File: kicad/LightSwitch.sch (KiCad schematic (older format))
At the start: 20 parts

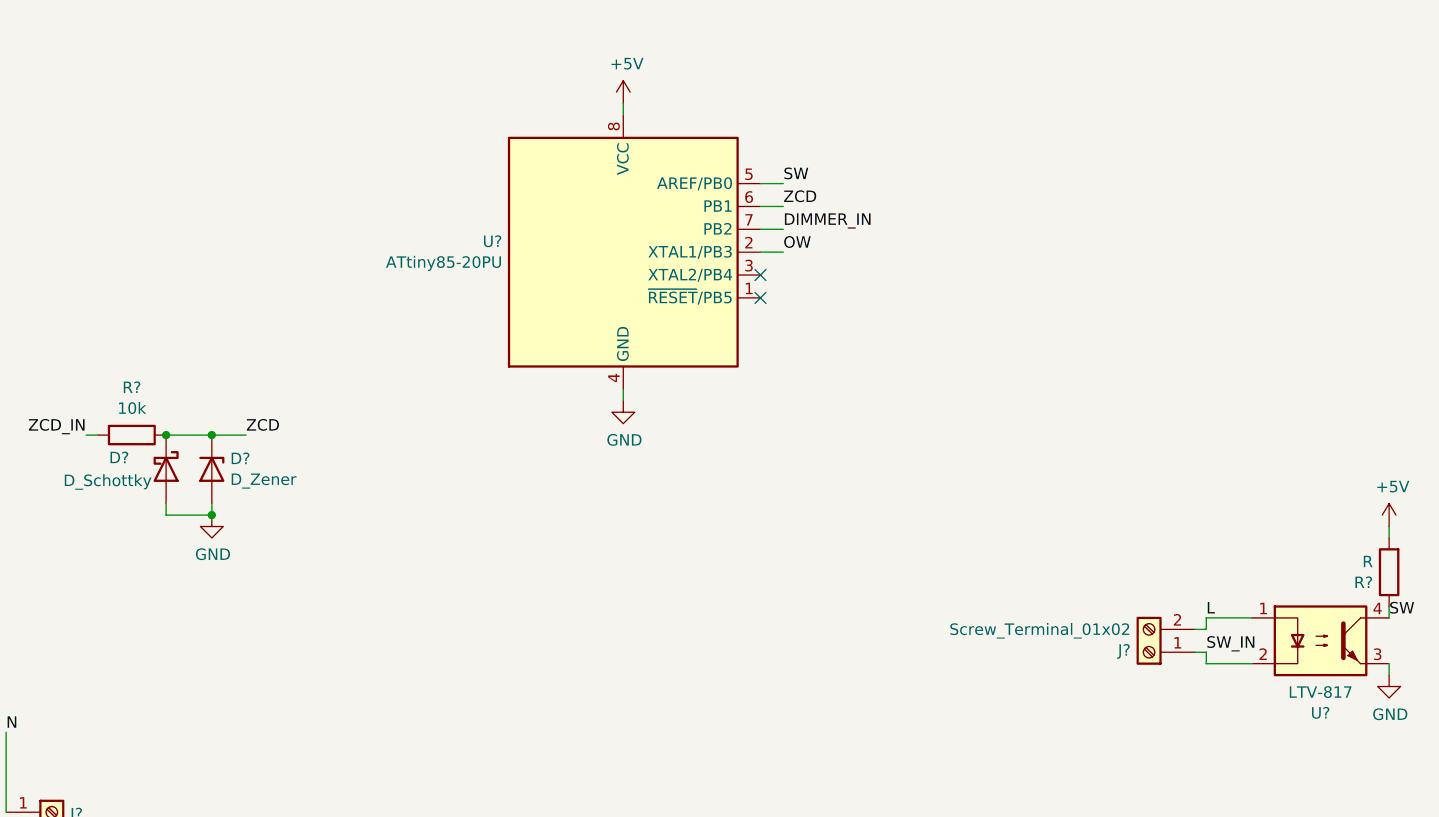
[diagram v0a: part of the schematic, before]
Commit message: Some small circuit changes
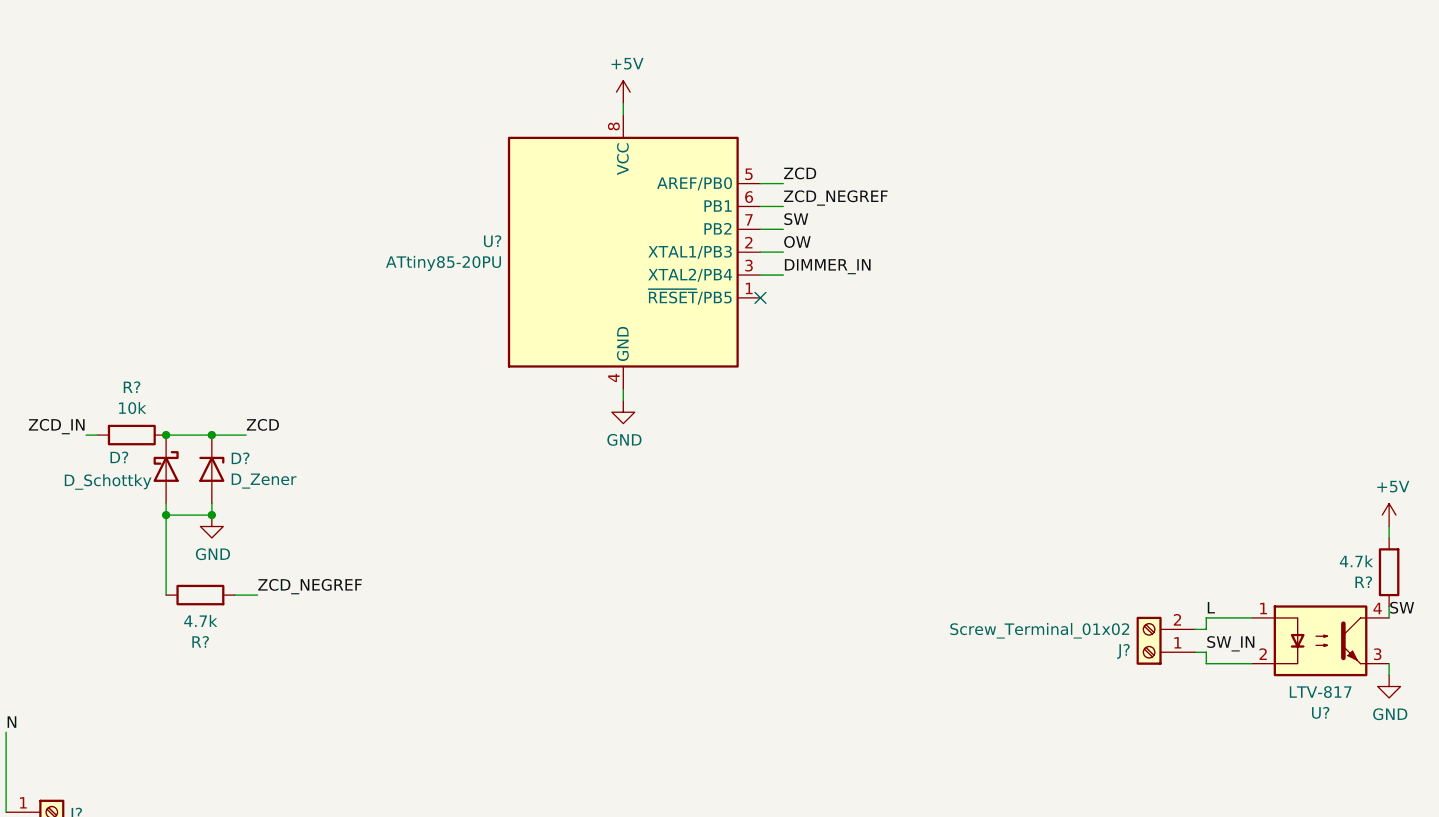
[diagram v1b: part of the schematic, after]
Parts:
- added R?: 4.7k, symbol Device:R
- R?: value R -> 4.7k
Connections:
- net DIMMER_IN: now also U?.3 (XTAL2/PB4); no longer U?.7 (PB2)
- net GND: now also R?.1
- net SW: now also U?.7 (PB2); no longer U?.5 (AREF/PB0)
- net ZCD: now also U?.5 (AREF/PB0); no longer U?.6 (PB1)
- new net ZCD_NEGREF: R?.2, U?.6 (PB1)
- no-connect marks 2 -> 1
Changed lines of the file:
@@
 Wire Wire Line
 	6650 1250 6650 1300
+Text Label 7350 1800 0    50   ~ 0
+SW
+Wire Wire Line
+	7250 1600 7350 1600
 Text Label 7350 1600 0    50   ~ 0
-SW
-Wire Wire Line
-	7250 1600 7350 1600
-Text Label 7350 1700 0    50   ~ 0
 ZCD
-Wire Wire Line
-	7350 1700 7250 1700
 $Comp
 L Relay_SolidState:MOC3052M U?
@@
 Wire Wire Line
 	2000 4250 2050 4250
-Text Label 7350 1800 0    50   ~ 0
+Text Label 7350 2000 0    50   ~ 0
 DIMMER_IN
 Wire Wire Line
@@
 	7350 1900 7250 1900
 NoConn ~ 7250 2100
-NoConn ~ 7250 2000
 $Comp
 L Connector:Screw_Terminal_01x02 J?
@@
 P 10000 3300
 F 0 "R?" H 10070 3346 50  0000 L CNN
-F 1 "R" H 10070 3255 50  0000 L CNN
+F 1 "4.7k" H 10070 3255 50  0000 L CNN
 F 2 "" V 9930 3300 50  0001 C CNN
 F 3 "~" H 10000 3300 50  0001 C CNN
@@
 Wire Wire Line
 	4850 2700 5000 2700
+$Comp
+L Device:R R?
+U 1 1 61ADD4D7
+P 4800 3400
+F 0 "R?" V 4593 3400 50  0000 C CNN
+F 1 "4.7k" V 4684 3400 50  0000 C CNN
+F 2 "" V 4730 3400 50  0001 C CNN
+F 3 "~" H 4800 3400 50  0001 C CNN
+	1    4800 3400
+	0    -1   -1   0
+$EndComp
+Wire Wire Line
+	4650 3050 4650 3400
+Wire Wire Line
+	7250 1700 7350 1700
+Wire Wire Line
+	7350 2000 7250 2000
+Wire Wire Line
+	4950 3400 5050 3400
+Text Label 5050 3400 0    50   ~ 0
+ZCD_NEGREF
+Text Label 7350 1700 0    50   ~ 0
+ZCD_NEGREF
+Connection ~ 4650 3050
 $EndSCHEMATC

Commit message: more circuit changes
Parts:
- removed D?: D, symbol Device:D
- removed U?: L7805, symbol Regulator_Linear:L7805
- added J?: Screw_Terminal_01x03, symbol Connector:Screw_Terminal_01x03
- added R?: R, symbol Device:R
- added U?: LM2936-5.0, symbol Regulator_Linear:LM2936-5.0
- C1: renamed from C?; value 2200u -> 470u
- C2: renamed from C?; value 0.1u -> 10u
- gave numbers to parts that had none: 17
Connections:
- net +5V: now also U?.3 (VO)
- net GND: now also J?.3 (Pin_3), U?.2 (GND)
- net L: now also J3.1 (Pin_1); no longer J3.2 (Pin_2), U3.1
- net N: now also U3.2
- net SW_IN: now also J3.2 (Pin_2), R?.1; no longer J3.1 (Pin_1), U3.2
- net at C1.1, D1.1 (K), D2.1 (K): now also U?.1 (VI)
- net DIMMER_LV: now reaches U4.1 (~RESET~/PB5)
- net DIMMER_LV: now also R1.2
- net DIMMER_IN renamed ALERT
- net ALERT: now also J?.2 (Pin_2); no longer R1.2
- net OW renamed ONEWIRE
- net ONEWIRE: now also J?.1 (Pin_1)
- net PWR_OUT renamed LIGHT
- net ZCD_NEGREF renamed ZCD_NEG
- new net: R?.2, U3.1
- no-connect marks 1 -> 0
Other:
- moved on the sheet: C1, C2, D1, D2, J2, J3, Q1, R1, R2, R4, R5, U1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
